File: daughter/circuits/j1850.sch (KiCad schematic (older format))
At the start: 7 parts, among them U12 LTV-827S

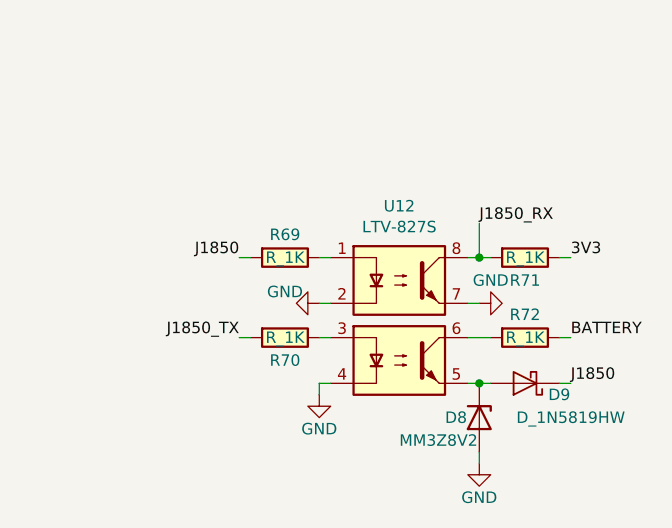
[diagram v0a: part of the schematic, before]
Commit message: 0) Switched to h-bridge drivers for hvac 1) Connected ignition sense io 2) MCP config pins and reset 3) Fixed usb resistors 4) Fixed BJT footprint 5) Added car interface pcb for C6 Corvette
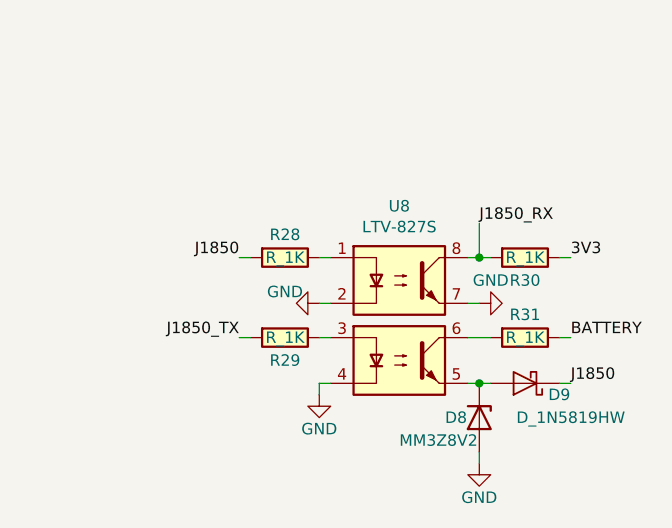
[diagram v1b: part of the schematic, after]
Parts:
- renumbered R69 to R28, R70 to R29, R71 to R30, R72 to R31, U12 to U8
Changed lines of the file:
@@
 $Descr A4 11693 8268
 encoding utf-8
-Sheet 4 8
+Sheet 4 14
 Title ""
 Date ""
@@
 P 6050 2750
 AR Path="/5FBF1F61/5FD18EDF" Ref="U?"  Part="1"
-AR Path="/6063934A/5FD18EDF" Ref="U12"  Part="1"
-F 0 "U12" H 6050 3275 50  0000 C CNN
+AR Path="/6063934A/5FD18EDF" Ref="U8"  Part="1"
+F 0 "U8" H 6050 3275 50  0000 C CNN
 F 1 "LTV-827S" H 6050 3184 50  0000 C CNN
 F 2 "Package_DIP:SMDIP-8_W9.53mm" H 6000 3300 50  0001 C CNN
@@
 AR Path="/5FBF1F61/5FD18EF7" Ref="#PWR?"  Part="1"
 AR Path="/5FFBD8EA/5FD18EF7" Ref="#PWR?"  Part="1"
-AR Path="/6063934A/5FD18EF7" Ref="#PWR082"  Part="1"
-F 0 "#PWR082" H 5700 2400 50  0001 C CNN
+AR Path="/6063934A/5FD18EF7" Ref="#PWR068"  Part="1"
+F 0 "#PWR068" H 5700 2400 50  0001 C CNN
 F 1 "GND" V 5650 2500 50  0000 C CNN
 F 2 "" H 5700 2650 50  0000 C CNN
@@
 AR Path="/5FBF1F61/5FD18EFD" Ref="#PWR?"  Part="1"
 AR Path="/5FFBD8EA/5FD18EFD" Ref="#PWR?"  Part="1"
-AR Path="/6063934A/5FD18EFD" Ref="#PWR083"  Part="1"
-F 0 "#PWR083" H 5700 2800 50  0001 C CNN
+AR Path="/6063934A/5FD18EFD" Ref="#PWR069"  Part="1"
+F 0 "#PWR069" H 5700 2800 50  0001 C CNN
 F 1 "GND" H 5700 2900 50  0000 C CNN
 F 2 "" H 5700 3050 50  0000 C CNN
@@
 AR Path="/5FBF1F61/5FD18F10" Ref="#PWR?"  Part="1"
 AR Path="/5FFBD8EA/5FD18F10" Ref="#PWR?"  Part="1"
-AR Path="/6063934A/5FD18F10" Ref="#PWR084"  Part="1"
-F 0 "#PWR084" H 6400 2400 50  0001 C CNN
+AR Path="/6063934A/5FD18F10" Ref="#PWR070"  Part="1"
+F 0 "#PWR070" H 6400 2400 50  0001 C CNN
 F 1 "GND" V 6500 2600 50  0000 C CNN
 F 2 "" H 6400 2650 50  0000 C CNN
@@
 J1850
 $Comp
-L open-dash-daughterboard-rescue:R_1K-Open_Automation R69
+L open-dash-daughterboard-rescue:R_1K-Open_Automation R28
 U 1 1 5FD1CF29
 P 5550 2450
-F 0 "R69" V 5450 2450 50  0000 C CNN
+F 0 "R28" V 5450 2450 50  0000 C CNN
 F 1 "R_1K" V 5550 2450 50  0000 C CNN
 F 2 "Resistor_SMD:R_0603_1608Metric_Pad0.98x0.95mm_HandSolder" V 5480 2450 50  0001 C CNN
@@
 J1850_TX
 $Comp
-L open-dash-daughterboard-rescue:R_1K-Open_Automation R70
+L open-dash-daughterboard-rescue:R_1K-Open_Automation R29
 U 1 1 5FD20151
 P 5550 2800
-F 0 "R70" V 5650 2800 50  0000 C CNN
+F 0 "R29" V 5650 2800 50  0000 C CNN
 F 1 "R_1K" V 5550 2800 50  0000 C CNN
 F 2 "Resistor_SMD:R_0603_1608Metric_Pad0.98x0.95mm_HandSolder" V 5480 2800 50  0001 C CNN
@@
 	6350 2800 6450 2800
 $Comp
-L open-dash-daughterboard-rescue:R_1K-Open_Automation R72
+L open-dash-daughterboard-rescue:R_1K-Open_Automation R31
 U 1 1 5FD34872
 P 6600 2800
-F 0 "R72" V 6500 2800 50  0000 C CNN
+F 0 "R31" V 6500 2800 50  0000 C CNN
 F 1 "R_1K" V 6600 2800 50  0000 C CNN
 F 2 "Resistor_SMD:R_0603_1608Metric_Pad0.98x0.95mm_HandSolder" V 6530 2800 50  0001 C CNN
@@
 AR Path="/5FBF1F61/5FD3E587" Ref="#PWR?"  Part="1"
 AR Path="/5FFBD8EA/5FD3E587" Ref="#PWR?"  Part="1"
-AR Path="/6063934A/5FD3E587" Ref="#PWR085"  Part="1"
-F 0 "#PWR085" H 6400 3100 50  0001 C CNN
+AR Path="/6063934A/5FD3E587" Ref="#PWR071"  Part="1"
+F 0 "#PWR071" H 6400 3100 50  0001 C CNN
 F 1 "GND" H 6400 3200 50  0000 C CNN
 F 2 "" H 6400 3350 50  0000 C CNN
@@
 $EndComp
 $Comp
-L open-dash-daughterboard-rescue:R_1K-Open_Automation R71
+L open-dash-daughterboard-rescue:R_1K-Open_Automation R30
 U 1 1 5FD45435
 P 6600 2450
-F 0 "R71" V 6700 2450 50  0000 C CNN
+F 0 "R30" V 6700 2450 50  0000 C CNN
 F 1 "R_1K" V 6600 2450 50  0000 C CNN
 F 2 "Resistor_SMD:R_0603_1608Metric_Pad0.98x0.95mm_HandSolder" V 6530 2450 50  0001 C CNN

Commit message: sent v1.2 to fab
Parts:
- removed D9: D_1N5819HW, Diode_SMD:D_SOD-123, symbol open-dash-daughterboard-rescue:D_1N5819HW-Open_Automation
- removed U8: LTV-827S, Package_DIP:SMDIP-8_W9.53mm, symbol open-dash-daughterboard-rescue:LTV-827S-Open_Automation
- added D9: D_1N5819HW, Diode_SMD:D_SOD-123, symbol Open_Automation:D_1N5819HW
- added U8: Opto_TLP521, Package_DIP:SMDIP-8_W9.53mm, symbol Open_Automation:Opto_TLP521
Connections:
- net GND: now also U8.2, U8.4, U8.7
- net J1850: now also D9.1 (K)
- net J1850_RX: now also U8.8
- net at R28.1: now also U8.1
- net at R29.1: now also U8.3
- net at D8.1 (K): now also D9.2 (A), U8.5
- net at R31.2: now also U8.6
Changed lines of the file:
@@
 	1250 1050 1200 1050
-$Comp
-L open-dash-daughterboard-rescue:LTV-827S-Open_Automation U?
-U 1 1 5FD18EDF
-P 6050 2750
-AR Path="/5FBF1F61/5FD18EDF" Ref="U?"  Part="1"
-AR Path="/6063934A/5FD18EDF" Ref="U8"  Part="1"
-F 0 "U8" H 6050 3275 50  0000 C CNN
-F 1 "LTV-827S" H 6050 3184 50  0000 C CNN
-F 2 "Package_DIP:SMDIP-8_W9.53mm" H 6000 3300 50  0001 C CNN
-F 3 "https://datasheet.lcsc.com/szlcsc/1811092010_Lite-On-LTV-827S-TA1_C22112.pdf" H 5950 3150 50  0001 C CNN
-F 4 "LTV-827S-TA1" H 6000 3400 50  0001 C CNN "Part Number"
-F 5 "C22112" H 0   0   50  0001 C CNN "LCSC"
-	1    6050 2750
-	1    0    0    -1
-$EndComp
 $Comp
 L open-dash-daughterboard-rescue:GND-open-automation #PWR?
@@
 	6800 3000 6750 3000
 $Comp
-L open-dash-daughterboard-rescue:D_1N5819HW-Open_Automation D?
-U 1 1 5FD3E56E
-P 6600 3000
-AR Path="/5FD3E56E" Ref="D?"  Part="1"
-AR Path="/6063934A/5FD3E56E" Ref="D9"  Part="1"
-F 0 "D9" H 6450 3050 50  0000 C CNN
-F 1 "D_1N5819HW" H 6400 3150 50  0000 C CNN
-F 2 "Diode_SMD:D_SOD-123" H 6600 2825 50  0001 C CNN
-F 3 "http://www.diodes.com/_files/datasheets/ds23022.pdf" H 6600 3000 50  0001 C CNN
-F 4 "https://www.digikey.com/product-detail/en/diodes-incorporated/1N5819HW-7-F/1N5819HW-FDICT-ND/815283" H 6700 3200 50  0001 C CNN "Website"
-F 5 "1N5819HW-7-F" H 6600 3300 50  0001 C CNN "Part Number"
-F 6 "C117948" H 6600 3000 50  0001 C CNN "LCSC"
-	1    6600 3000
-	-1   0    0    1
-$EndComp
-$Comp
 L open-dash-daughterboard-rescue:MM3Z8V2-Open_Automation D8
 U 1 1 5FD3E57A
@@
 	0    1    1    0
 $EndComp
+$Comp
+L Open_Automation:Opto_TLP521 U?
+U 1 1 6066A554
+P 6050 2750
+AR Path="/5A7BADB8/6066A554" Ref="U?"  Part="1"
+AR Path="/6063934A/6066A554" Ref="U8"  Part="1"
+F 0 "U8" H 6050 3275 50  0000 C CNN
+F 1 "Opto_TLP521" H 6050 3184 50  0000 C CNN
+F 2 "Package_DIP:SMDIP-8_W9.53mm" H 6000 3300 50  0001 C CNN
+F 3 "https://datasheet.lcsc.com/szlcsc/2009251934_Isocom-Components-TLP521-2SMT-R_C722233.pdf" H 5950 3150 50  0001 C CNN
+F 4 "TLP521-2SMT&R" H 6000 3400 50  0001 C CNN "Part Number"
+F 5 "C722233" H 6000 3500 50  0001 C CNN "LCSC"
+	1    6050 2750
+	1    0    0    -1
+$EndComp
+$Comp
+L Open_Automation:D_1N5819HW D9
+U 1 1 6076C81A
+P 6600 3000
+F 0 "D9" H 6500 2950 50  0000 C CNN
+F 1 "D_1N5819HW" H 6450 3100 50  0000 C CNN
+F 2 "Diode_SMD:D_SOD-123" H 6600 2825 50  0001 C CNN
+F 3 "https://datasheet.lcsc.com/szlcsc/Diodes-Incorporated-1N5819HW-7-F_C82544.pdf" H 6600 3000 50  0001 C CNN
+F 4 "1N5819HW-7-F" H 6600 3300 50  0001 C CNN "Part Number"
+F 5 "C82544" H 6600 3400 50  0001 C CNN "LCSC"
+	1    6600 3000
+	-1   0    0    1
+$EndComp
 $EndSCHEMATC

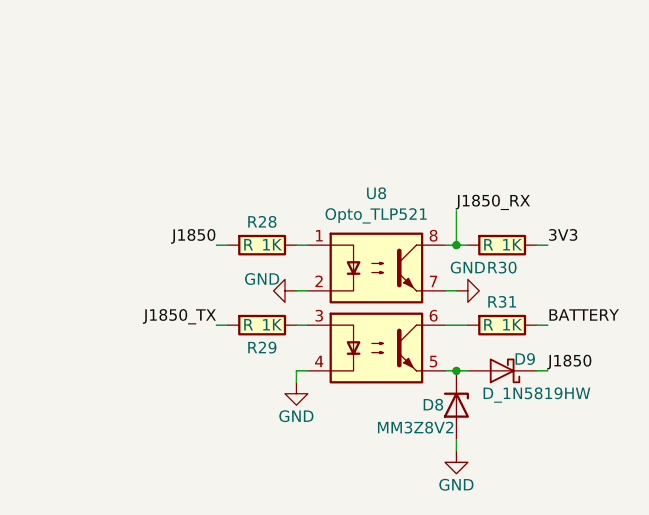
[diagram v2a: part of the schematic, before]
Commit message: Added external amp trigger code and circuit to PCB. Made some layout modifications.
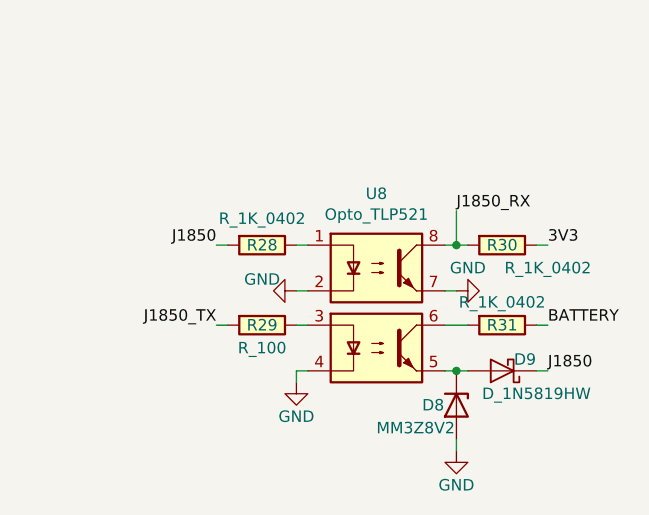
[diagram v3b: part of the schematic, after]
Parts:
- removed R28, R29, R30, R31: R_1K, Resistor_SMD:R_0603_1608Metric_Pad0.98x0.95mm_HandSolder, symbol open-dash-daughterboard-rescue:R_1K-Open_Automation
- added R28, R30, R31: R_1K_0402, Resistor_SMD:R_0402_1005Metric_Pad0.72x0.64mm_HandSolder, symbol Open_Automation:R_1K_0402
- added R29: R_100, Resistor_SMD:R_0402_1005Metric_Pad0.72x0.64mm_HandSolder, symbol Open_Automation:R_100
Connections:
- net 3V3: now also R30.1
- net BATTERY: now also R31.1
- net J1850: now also R28.2
- net J1850_RX: now also R30.2
- net J1850_TX: now also R29.1
- net at U8.1: now also R28.1
- net at U8.3: now also R29.2
- net at U8.6: now also R31.2
